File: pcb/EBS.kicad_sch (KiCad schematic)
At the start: 21 parts, among them Q1 BC547, Q2 BC557

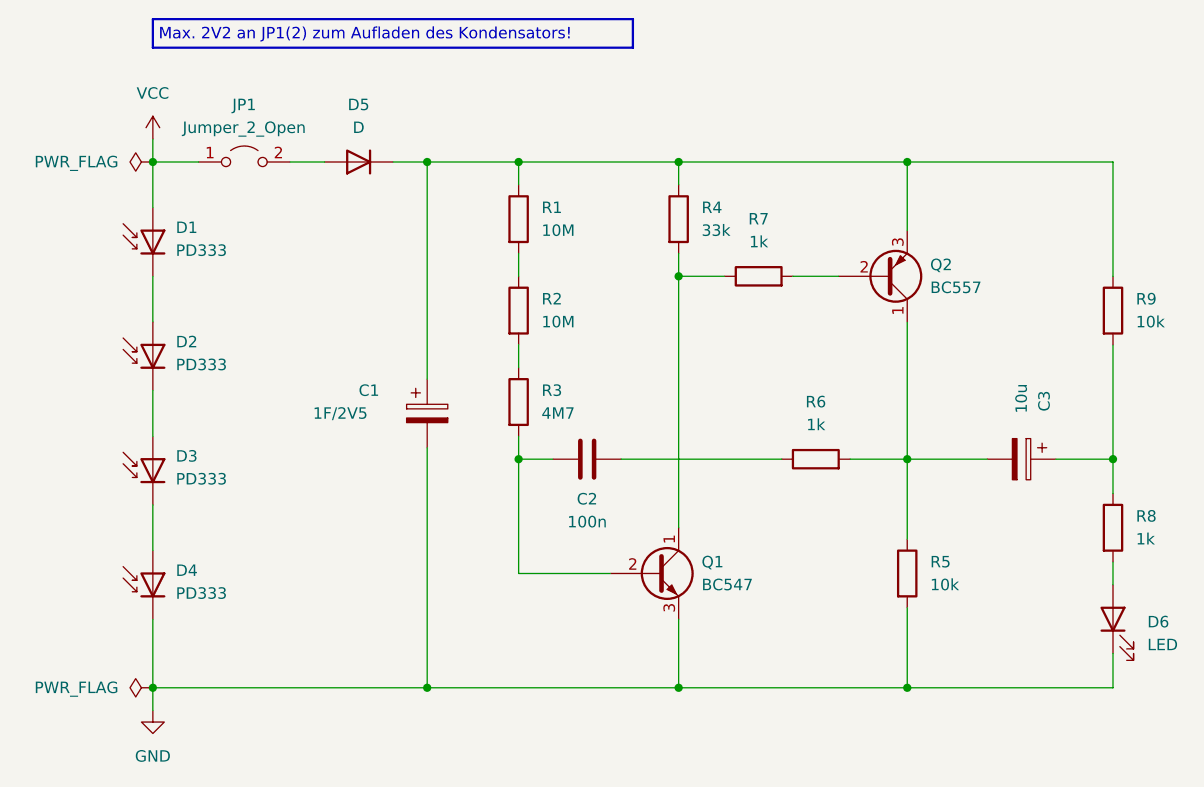
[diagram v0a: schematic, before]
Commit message: Change resistor unit
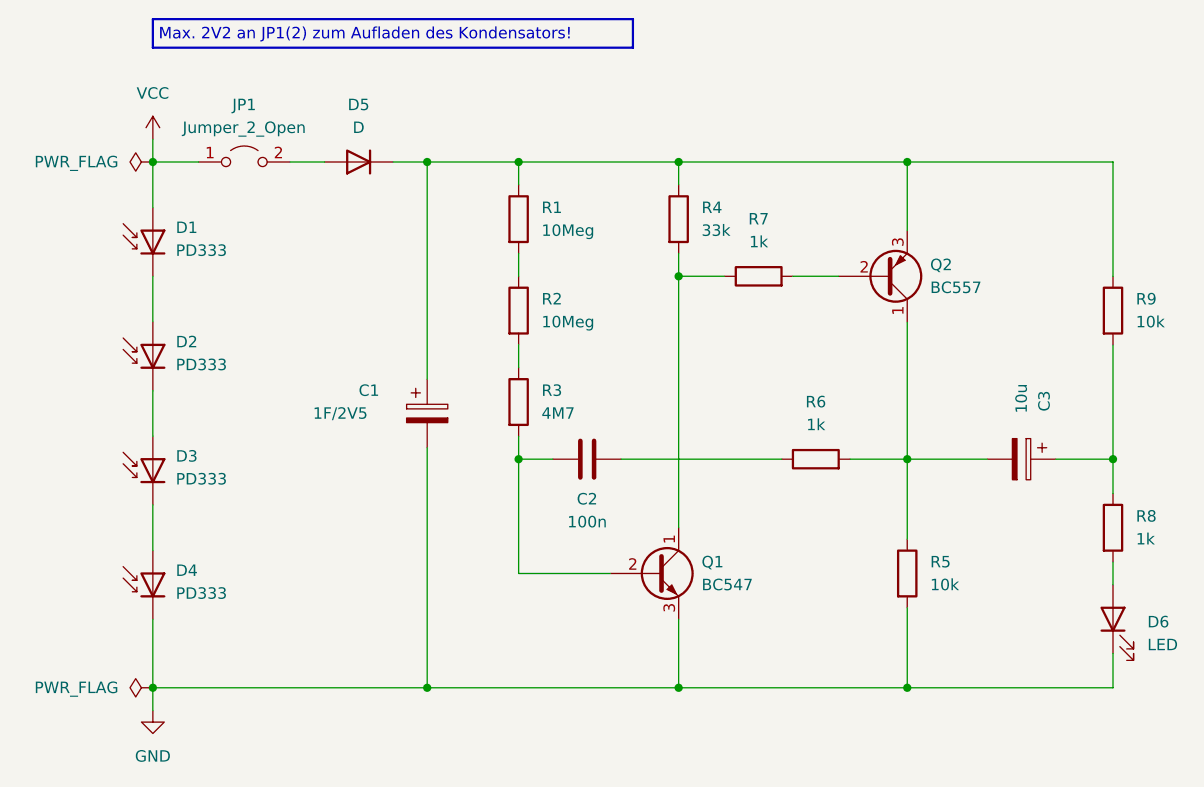
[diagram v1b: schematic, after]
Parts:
- R1, R2: value 10M -> 10Meg
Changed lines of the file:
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@@
   (symbol (lib_id "Device:R") (at 142.24 80.01 0) (unit 1)
     (in_bom yes) (on_board yes) (dnp no) (fields_autoplaced)
-    (property "Reference" "R2" (at 144.78 78.7399 0)
+    (property "Reference" "R2" (at 144.78 78.74 0)
       (effects (font (size 1.27 1.27)) (justify left))
     )
-    (property "Value" "10M" (at 144.78 81.2799 0)
+    (property "Value" "10Meg" (at 144.78 81.28 0)
       (effects (font (size 1.27 1.27)) (justify left))
     )
@@
   (symbol (lib_id "Device:R") (at 142.24 69.85 0) (unit 1)
     (in_bom yes) (on_board yes) (dnp no) (fields_autoplaced)
-    (property "Reference" "R1" (at 144.78 68.5799 0)
+    (property "Reference" "R1" (at 144.78 68.58 0)
       (effects (font (size 1.27 1.27)) (justify left))
     )
-    (property "Value" "10M" (at 144.78 71.1199 0)
+    (property "Value" "10Meg" (at 144.78 71.12 0)
       (effects (font (size 1.27 1.27)) (justify left))
     )

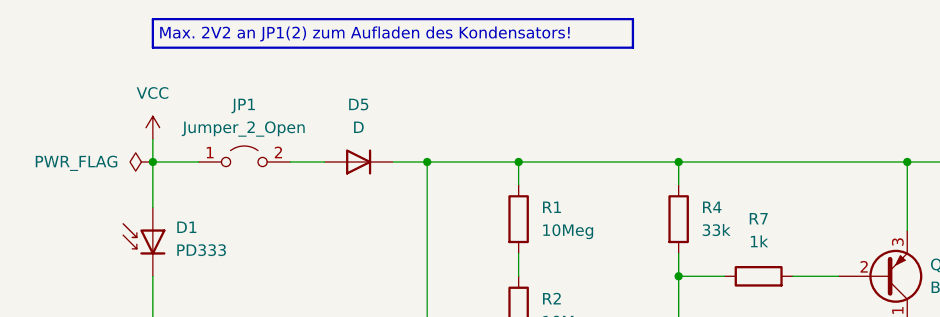
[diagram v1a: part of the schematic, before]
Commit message: Extend information text
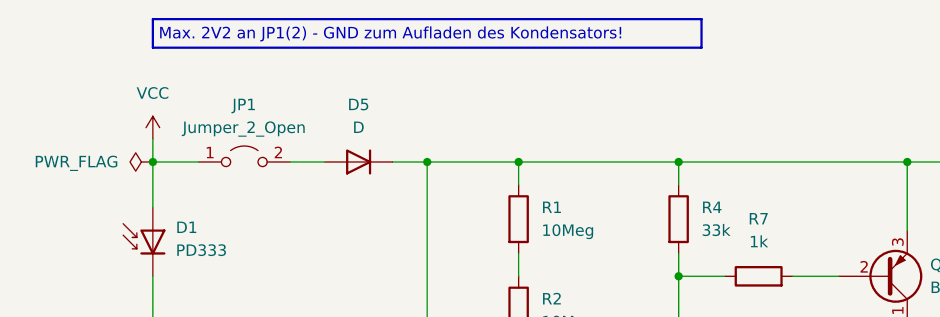
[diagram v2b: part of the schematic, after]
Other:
- note added: "Max. 2V2 an JP1(2) - GND zum Aufladen des Kondensators!"
- note removed: "Max. 2V2 an JP1(2) zum Aufladen des Kondensators!"
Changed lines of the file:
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@@
     (stroke (width 0) (type default))
   )
-  (polyline (pts (xy 154.94 47.625) (xy 154.94 50.8))
+  (polyline (pts (xy 162.56 47.625) (xy 162.56 50.8))
     (stroke (width 0.25) (type solid) (color 31 0 255 1))
   )
@@
     (stroke (width 0) (type default))
   )
-  (polyline (pts (xy 154.94 50.8) (xy 101.6 50.8))
+  (polyline (pts (xy 162.56 50.8) (xy 101.6 50.8))
     (stroke (width 0.25) (type solid) (color 31 0 255 1))
   )
@@
     (stroke (width 0) (type default))
   )
-  (polyline (pts (xy 101.6 47.625) (xy 154.94 47.625))
+  (polyline (pts (xy 101.6 47.625) (xy 162.56 47.625))
     (stroke (width 0.25) (type solid) (color 31 0 255 1))
   )
@@
     (stroke (width 0) (type default))
   )
-  (text "Max. 2V2 an JP1(2) zum Aufladen des Kondensators!" (at 102.235 50.165 0)
+  (text "Max. 2V2 an JP1(2) - GND zum Aufladen des Kondensators!"
+    (at 102.235 50.165 0)
     (effects (font (size 1.27 1.27)) (justify left bottom))
   )

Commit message: Fix BOM integration
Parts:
- C1: Hersteller HTL -> (none); Nummer 103397 -> (none); Vendor (none) -> HTL; VendorId (none) -> 103397
- C2: Hersteller HTL -> (none); Nummer 103390 -> (none); Vendor (none) -> HTL; VendorId (none) -> 103390
- C3: Hersteller HTL -> (none); Nummer 100353 -> (none); Vendor (none) -> HTL; VendorId (none) -> 100353
- D1, D2, D3, D4: Hersteller HTL -> (none); Nummer 103396 -> (none); Vendor (none) -> HTL; VendorId (none) -> 103396
- D5: Hersteller HTL -> (none); Nummer 100179 -> (none); Vendor (none) -> HTL; VendorId (none) -> 100179
- D6: Hersteller HTL -> (none); Nummer 100444 -> (none); Vendor (none) -> HTL; VendorId (none) -> 100444
- JP1: Hersteller HTL -> (none); Nummer 101521 -> (none); Vendor (none) -> HTL; VendorId (none) -> 101521
- Q1: Hersteller HTL -> (none); Nummer 100215 -> (none); Vendor (none) -> HTL; VendorId (none) -> 100215
- Q2: Hersteller HTL -> (none); Nummer 100219 -> (none); Vendor (none) -> HTL; VendorId (none) -> 100219
- R1, R2: Hersteller HTL -> (none); Nummer 102845 -> (none); Vendor (none) -> HTL; VendorId (none) -> 102845
- R3: Hersteller HTL -> (none); Nummer 102844 -> (none); Vendor (none) -> HTL; VendorId (none) -> 102844
- R4: Hersteller HTL -> (none); Nummer 102818 -> (none); Vendor (none) -> HTL; VendorId (none) -> 102818
- R5, R9: Hersteller HTL -> (none); Nummer 102812 -> (none); Vendor (none) -> HTL; VendorId (none) -> 102812
- R6, R7, R8: Hersteller HTL -> (none); Nummer 102800 -> (none); Vendor (none) -> HTL; VendorId (none) -> 102800
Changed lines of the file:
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@@
       (effects (font (size 1.27 1.27)) hide)
     )
-    (property "Hersteller" "HTL" (at 101.6 83.82 0)
-      (effects (font (size 1.27 1.27)) hide)
-    )
-    (property "Nummer" "103396" (at 101.6 83.82 0)
+    (property "Vendor" "HTL" (at 101.6 83.82 0)
+      (effects (font (size 1.27 1.27)) hide)
+    )
+    (property "VendorId" "103396" (at 101.6 83.82 0)
       (effects (font (size 1.27 1.27)) hide)
     )
@@
       (effects (font (size 1.27 1.27)) hide)
     )
-    (property "Hersteller" "HTL" (at 124.46 63.5 0)
-      (effects (font (size 1.27 1.27)) hide)
-    )
-    (property "Nummer" "100179" (at 124.46 63.5 0)
+    (property "Vendor" "HTL" (at 124.46 63.5 0)
+      (effects (font (size 1.27 1.27)) hide)
+    )
+    (property "VendorId" "100179" (at 124.46 63.5 0)
       (effects (font (size 1.27 1.27)) hide)
     )
@@
       (effects (font (size 1.27 1.27)) (justify left) hide)
     )
-    (property "Hersteller" "HTL" (at 182.88 76.2 0)
-      (effects (font (size 1.27 1.27)) hide)
-    )
-    (property "Nummer" "100219" (at 182.88 76.2 0)
+    (property "Vendor" "HTL" (at 182.88 76.2 0)
+      (effects (font (size 1.27 1.27)) hide)
+    )
+    (property "VendorId" "100219" (at 182.88 76.2 0)
       (effects (font (size 1.27 1.27)) hide)
     )
@@
       (effects (font (size 1.27 1.27)) hide)
     )
-    (property "Hersteller" "HTL" (at 185.42 109.22 0)
-      (effects (font (size 1.27 1.27)) hide)
-    )
-    (property "Nummer" "102812" (at 185.42 109.22 0)
+    (property "Vendor" "HTL" (at 185.42 109.22 0)
+      (effects (font (size 1.27 1.27)) hide)
+    )
+    (property "VendorId" "102812" (at 185.42 109.22 0)
       (effects (font (size 1.27 1.27)) hide)
     )
@@
       (effects (font (size 1.27 1.27)) hide)
     )
-    (property "Hersteller" "HTL" (at 198.12 96.52 0)
-      (effects (font (size 1.27 1.27)) hide)
-    )
-    (property "Nummer" "100353" (at 198.12 96.52 0)
+    (property "Vendor" "HTL" (at 198.12 96.52 0)
+      (effects (font (size 1.27 1.27)) hide)
+    )
+    (property "VendorId" "100353" (at 198.12 96.52 0)
       (effects (font (size 1.27 1.27)) hide)
     )
@@
       (effects (font (size 1.27 1.27)) hide)
     )
-    (property "Hersteller" "HTL" (at 160.02 69.85 0)
-      (effects (font (size 1.27 1.27)) hide)
-    )
-    (property "Nummer" "102818" (at 160.02 69.85 0)
+    (property "Vendor" "HTL" (at 160.02 69.85 0)
+      (effects (font (size 1.27 1.27)) hide)
+    )
+    (property "VendorId" "102818" (at 160.02 69.85 0)
       (effects (font (size 1.27 1.27)) hide)
     )
@@
       (effects (font (size 1.27 1.27)) hide)
     )
-    (property "Hersteller" "HTL" (at 175.26 96.52 0)
-      (effects (font (size 1.27 1.27)) hide)
-    )
-    (property "Nummer" "102800" (at 175.26 96.52 0)
+    (property "Vendor" "HTL" (at 175.26 96.52 0)
+      (effects (font (size 1.27 1.27)) hide)
+    )
+    (property "VendorId" "102800" (at 175.26 96.52 0)
       (effects (font (size 1.27 1.27)) hide)
     )
@@
       (effects (font (size 1.27 1.27)) hide)
     )
-    (property "Hersteller" "HTL" (at 208.28 114.3 0)
-      (effects (font (size 1.27 1.27)) hide)
-    )
-    (property "Nummer" "100444" (at 208.28 114.3 0)
+    (property "Vendor" "HTL" (at 208.28 114.3 0)
+      (effects (font (size 1.27 1.27)) hide)
+    )
+    (property "VendorId" "100444" (at 208.28 114.3 0)
       (effects (font (size 1.27 1.27)) hide)
     )
@@
       (effects (font (size 1.27 1.27)) hide)
     )
-    (property "Hersteller" "HTL" (at 101.6 109.22 0)
-      (effects (font (size 1.27 1.27)) hide)
-    )
-    (property "Nummer" "103396" (at 101.6 109.22 0)
+    (property "Vendor" "HTL" (at 101.6 109.22 0)
+      (effects (font (size 1.27 1.27)) hide)
+    )
+    (property "VendorId" "103396" (at 101.6 109.22 0)
       (effects (font (size 1.27 1.27)) hide)
     )
@@
       (effects (font (size 1.27 1.27)) hide)
     )
-    (property "Hersteller" "HTL" (at 101.6 71.12 0)
-      (effects (font (size 1.27 1.27)) hide)
-    )
-    (property "Nummer" "103396" (at 101.6 71.12 0)
+    (property "Vendor" "HTL" (at 101.6 71.12 0)
+      (effects (font (size 1.27 1.27)) hide)
+    )
+    (property "VendorId" "103396" (at 101.6 71.12 0)
       (effects (font (size 1.27 1.27)) hide)
     )
@@
       (effects (font (size 1.27 1.27)) hide)
     )
-    (property "Hersteller" "HTL" (at 142.24 80.01 0)
-      (effects (font (size 1.27 1.27)) hide)
-    )
-    (property "Nummer" "102845" (at 142.24 80.01 0)
+    (property "Vendor" "HTL" (at 142.24 80.01 0)
+      (effects (font (size 1.27 1.27)) hide)
+    )
+    (property "VendorId" "102845" (at 142.24 80.01 0)
       (effects (font (size 1.27 1.27)) hide)
     )
@@
       (effects (font (size 1.27 1.27)) hide)
     )
-    (property "Hersteller" "HTL" (at 142.24 69.85 0)
-      (effects (font (size 1.27 1.27)) hide)
-    )
-    (property "Nummer" "102845" (at 142.24 69.85 0)
+    (property "Vendor" "HTL" (at 142.24 69.85 0)
+      (effects (font (size 1.27 1.27)) hide)
+    )
+    (property "VendorId" "102845" (at 142.24 69.85 0)
       (effects (font (size 1.27 1.27)) hide)
     )
@@
       (effects (font (size 1.27 1.27)) (justify left) hide)
     )
-    (property "Hersteller" "HTL" (at 157.48 109.22 0)
-      (effects (font (size 1.27 1.27)) hide)
-    )
-    (property "Nummer" "100215" (at 157.48 109.22 0)
+    (property "Vendor" "HTL" (at 157.48 109.22 0)
+      (effects (font (size 1.27 1.27)) hide)
+    )
+    (property "VendorId" "100215" (at 157.48 109.22 0)
       (effects (font (size 1.27 1.27)) hide)
     )
@@
       (effects (font (size 1.27 1.27)) hide)
     )
-    (property "Hersteller" "HTL" (at 132.08 91.44 0)
-      (effects (font (size 1.27 1.27)) hide)
-    )
-    (property "Nummer" "103397" (at 132.08 91.44 0)
+    (property "Vendor" "HTL" (at 132.08 91.44 0)
+      (effects (font (size 1.27 1.27)) hide)
+    )
+    (property "VendorId" "103397" (at 132.08 91.44 0)
       (effects (font (size 1.27 1.27)) hide)
     )
@@
       (effects (font (size 1.27 1.27)) hide)
     )
-    (property "Hersteller" "HTL" (at 142.24 90.17 0)
-      (effects (font (size 1.27 1.27)) hide)
-    )
-    (property "Nummer" "102844" (at 142.24 90.17 0)
+    (property "Vendor" "HTL" (at 142.24 90.17 0)
+      (effects (font (size 1.27 1.27)) hide)
+    )
+    (property "VendorId" "102844" (at 142.24 90.17 0)
       (effects (font (size 1.27 1.27)) hide)
     )
@@
       (effects (font (size 1.27 1.27)) hide)
     )
-    (property "Hersteller" "HTL" (at 149.86 96.52 0)
-      (effects (font (size 1.27 1.27)) hide)
-    )
-    (property "Nummer" "103390" (at 149.86 96.52 0)
+    (property "Vendor" "HTL" (at 149.86 96.52 0)
+      (effects (font (size 1.27 1.27)) hide)
+    )
+    (property "VendorId" "103390" (at 149.86 96.52 0)
       (effects (font (size 1.27 1.27)) hide)
     )
@@
       (effects (font (size 1.27 1.27)) hide)
     )
-    (property "Hersteller" "HTL" (at 208.28 104.14 0)
-      (effects (font (size 1.27 1.27)) hide)
-    )
-    (property "Nummer" "102800" (at 208.28 104.14 0)
+    (property "Vendor" "HTL" (at 208.28 104.14 0)
+      (effects (font (size 1.27 1.27)) hide)
+    )
+    (property "VendorId" "102800" (at 208.28 104.14 0)
       (effects (font (size 1.27 1.27)) hide)
     )
@@
       (effects (font (size 1.27 1.27)) hide)
     )
-    (property "Hersteller" "HTL" (at 111.76 63.5 0)
-      (effects (font (size 1.27 1.27)) hide)
-    )
-    (property "Nummer" "101521" (at 111.76 63.5 0)
+    (property "Vendor" "HTL" (at 111.76 63.5 0)
+      (effects (font (size 1.27 1.27)) hide)
+    )
+    (property "VendorId" "101521" (at 111.76 63.5 0)
       (effects (font (size 1.27 1.27)) hide)
     )
@@
       (effects (font (size 1.27 1.27)) hide)
     )
-    (property "Hersteller" "HTL" (at 168.91 76.2 0)
-      (effects (font (size 1.27 1.27)) hide)
-    )
-    (property "Nummer" "102800" (at 168.91 76.2 0)
+    (property "Vendor" "HTL" (at 168.91 76.2 0)
+      (effects (font (size 1.27 1.27)) hide)
+    )
+    (property "VendorId" "102800" (at 168.91 76.2 0)
       (effects (font (size 1.27 1.27)) hide)
     )
@@
       (effects (font (size 1.27 1.27)) hide)
     )
-    (property "Hersteller" "HTL" (at 101.6 96.52 0)
-      (effects (font (size 1.27 1.27)) hide)
-    )
-    (property "Nummer" "103396" (at 101.6 96.52 0)
+    (property "Vendor" "HTL" (at 101.6 96.52 0)
+      (effects (font (size 1.27 1.27)) hide)
+    )
+    (property "VendorId" "103396" (at 101.6 96.52 0)
       (effects (font (size 1.27 1.27)) hide)
     )
@@
       (effects (font (size 1.27 1.27)) hide)
     )
-    (property "Hersteller" "HTL" (at 208.28 80.01 0)
-      (effects (font (size 1.27 1.27)) hide)
-    )
-    (property "Nummer" "102812" (at 208.28 80.01 0)
-      (effects (font (size 1.27 1.27)) hide)
-    )
+    (property "Vendor" "HTL" (at 208.28 80.01 0)
+      (effects (font (size 1.27 1.27)) hide)
+    )
+    (property "VendorId" "102812" (at 208.28 80.01 0)
+      (effects (font (size 1.27 1.27)) hide)
+    )
